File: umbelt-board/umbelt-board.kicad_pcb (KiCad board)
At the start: 4 copper layers, 50.8 x 15.2 mm, 99 parts, among them J1 USB4105-GF-A, J2 Conn_01x06, J3 SM04B-SRSS-TB, J4 TC2050-IDC-NL, J5 BM02B-ACHLKS, J6 Conn_Flex_Motor, J7 Conn_Indiv_Motor, Q1 AO3415A, SW1 KMR231NG-ULC-LFS, SW2 CUS-12TB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

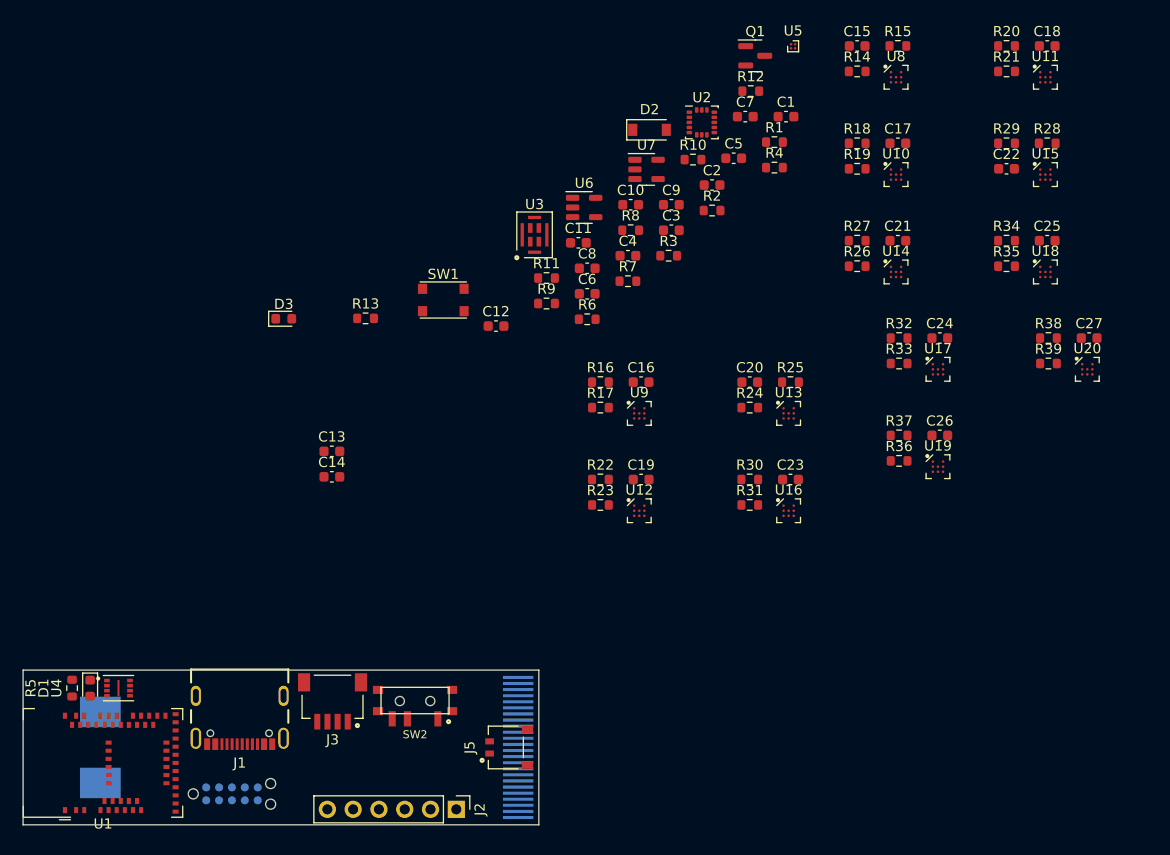
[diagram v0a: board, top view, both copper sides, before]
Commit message: more placement, update custom footprints' ref des on fab layer
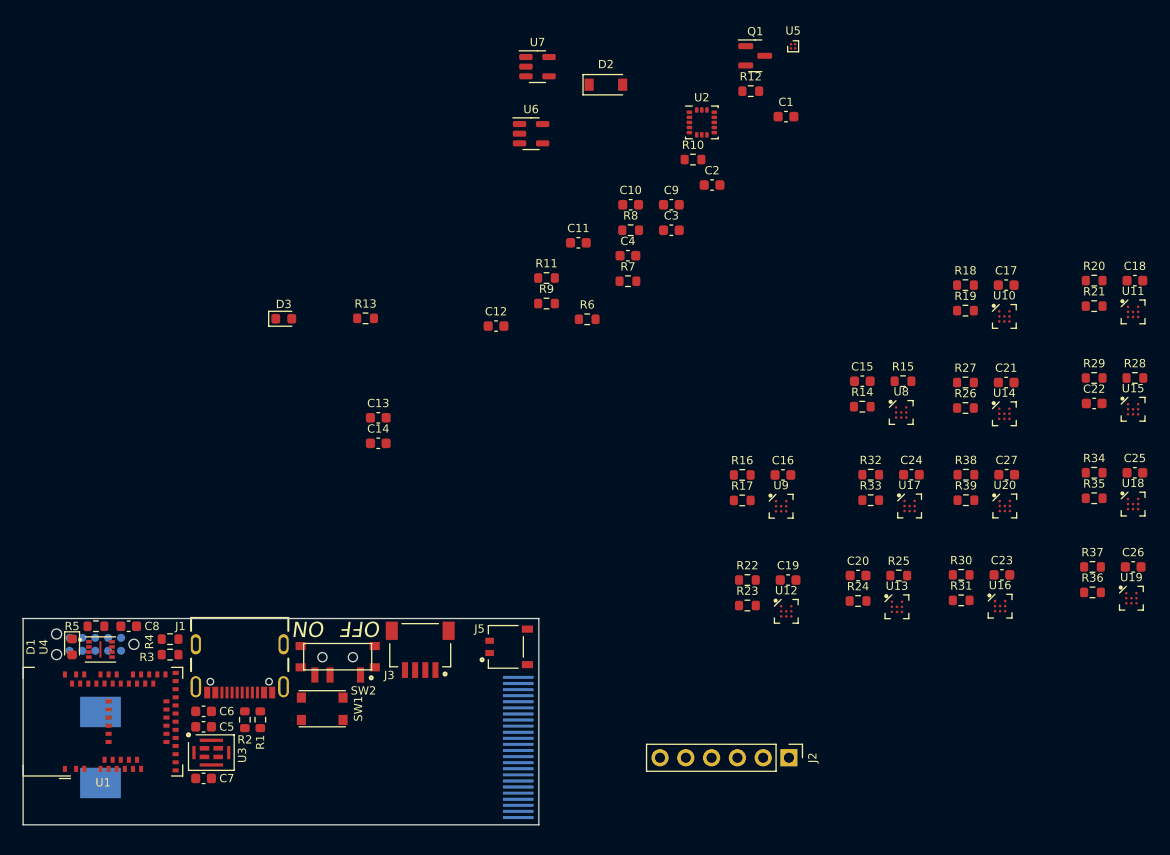
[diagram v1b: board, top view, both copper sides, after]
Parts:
- moved C7 84.2 mm to (144.8, 122.4)
- moved C5 76.6 mm to (144.8, 117.3)
- moved R1 76.2 mm to (150.4, 116.6), turned to 270 degrees
- moved R4 75.5 mm to (141.5, 108.7), turned to 180 degrees
- moved R2 68.1 mm to (148.8, 116.6), turned to 270 degrees
- moved R3 62.9 mm to (141.5, 110.2), turned to 180 degrees
- moved U3 60.1 mm to (145.5, 119.9), turned to 270 degrees
- moved C8 57.3 mm to (137.4, 107.4)
- moved C6 55.9 mm to (144.8, 115.8)
- moved SW1 42.0 mm to (156.5, 115.6)
- moved J2 33.2 mm to (202.4, 120.4)
- moved C15 33.0 mm to (209.7, 83.3)
- moved R15 33.0 mm to (213.7, 83.3)
- moved U8 33.0 mm to (213.5, 86.4)
- moved R14 33.0 mm to (209.7, 85.8)
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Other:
- board size 50.8 x 15.2 mm -> 50.8 x 20.3 mm
- board text added: "OFF"
- board text added: "ON"

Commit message: add SMD pin header, finished placement
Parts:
- J2: footprint Connector_PinHeader_2.54mm:PinHeader_1x06_P2.54mm_Vertical -> umbelt-board:PinHeader_1x06_P2.54mm_Right_Angle_SMD; moved to B.Cu
- moved U5 98.2 mm to (139.7, 125.5)
- moved C27 96.6 mm to (133.1, 125.5), turned to 90 degrees
- moved R38 94.2 mm to (131.6, 125.5), turned to 270 degrees
- moved C18 92.1 mm to (158.5, 122.4), turned to 90 degrees
- moved U20 91.8 mm to (136.9, 125.5), turned to 180 degrees
- moved R39 90.5 mm to (134.6, 125.5), turned to 270 degrees
- moved R20 90.0 mm to (157.0, 122.4), turned to 270 degrees
- moved U11 87.1 mm to (162.3, 122.4), turned to 180 degrees
- moved R21 86.1 mm to (160.0, 122.4), turned to 270 degrees
- moved C1 83.3 mm to (150.2, 122.4), turned to 270 degrees
- moved C17 83.3 mm to (158.5, 125.5), turned to 90 degrees
- moved R18 81.3 mm to (157.0, 125.5), turned to 270 degrees
- moved R15 80.8 mm to (144.8, 125.5), turned to 270 degrees
- moved C15 78.7 mm to (143.3, 125.5), turned to 90 degrees
- moved R14 78.7 mm to (141.7, 125.5), turned to 270 degrees
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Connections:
- net Net-(C12-Pad2) renamed /REGIN
- C10 pad 1: VBUS -> VBAT
- J5 pad 2: VBUS -> VBAT
- Q1 pad 2: VBUS -> VBAT
- R6 pad 1: VBUS -> VBAT
- U7 pad 3: VBUS -> VBAT
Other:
- board size 50.8 x 20.3 mm -> 56.6 x 20.3 mm
- board text added: "CHARGE"
- board text added: "RESET"
- board text added: "UMBELT"

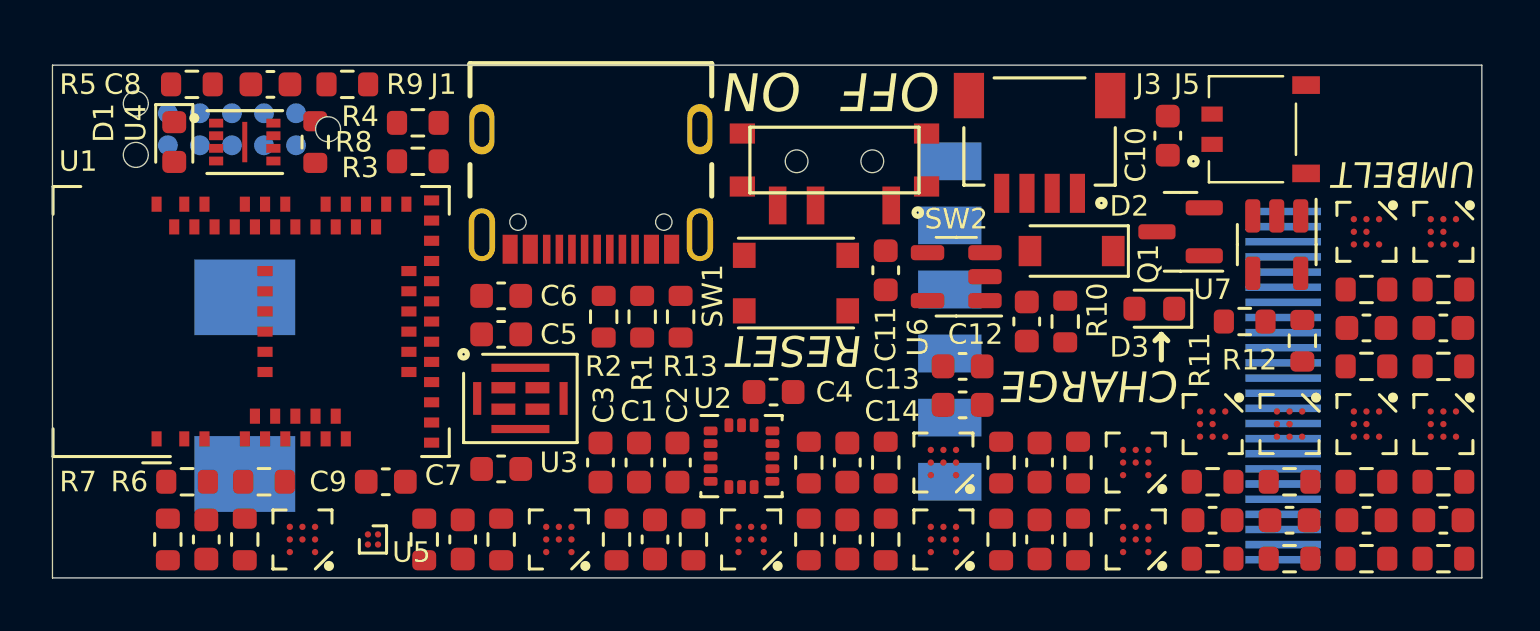
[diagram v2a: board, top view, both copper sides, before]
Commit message: tweak placement, add text, add test points, add rounded corners
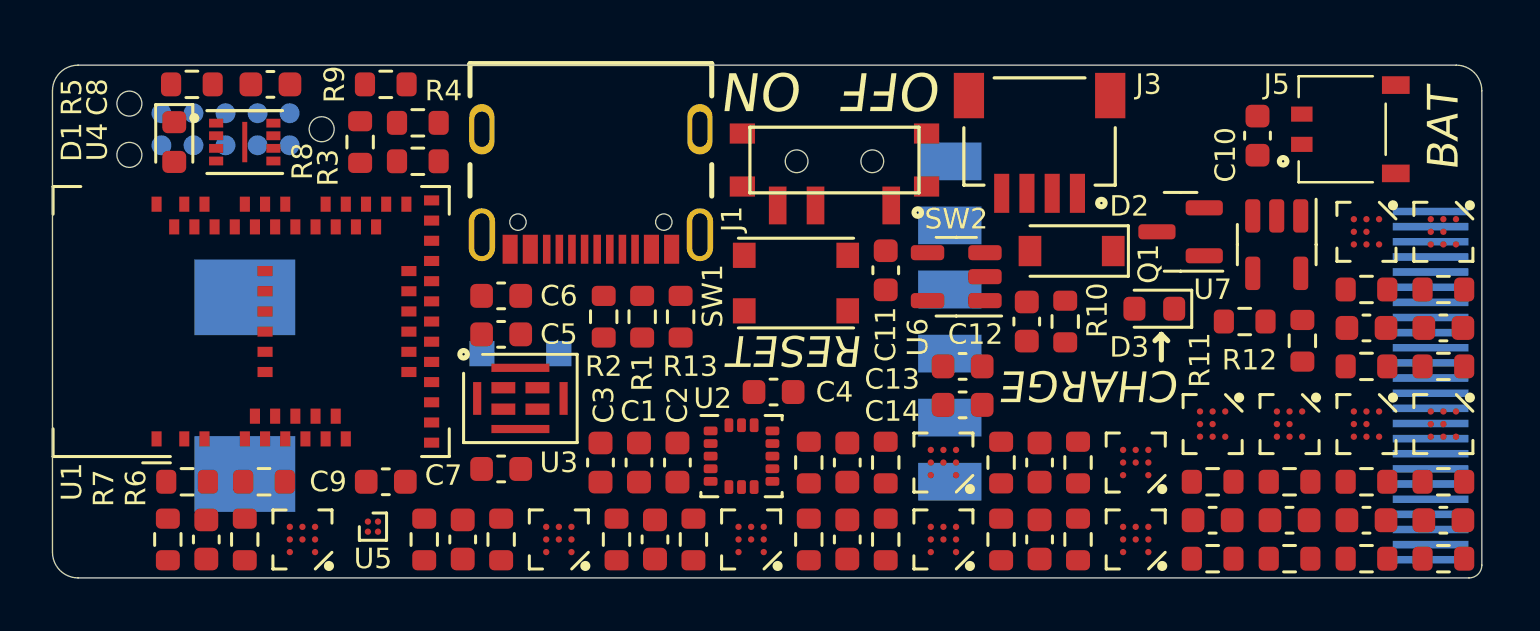
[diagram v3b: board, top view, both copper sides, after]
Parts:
- added TP1: PDM_DAT, TestPoint:TestPoint_Pad_1.0x1.0mm, B.Cu at (144.0, 118.1)
- added TP2: PDM_CLK, TestPoint:TestPoint_Pad_1.0x1.0mm, B.Cu at (147.1, 118.1)
- moved C23 7.62 mm to (179.1, 124.7)
- moved C24 7.62 mm to (182.1, 124.7)
- moved C25 7.62 mm to (179.1, 117.1)
- moved C26 7.62 mm to (182.1, 117.1)
- moved R30 7.62 mm to (179.1, 126.2)
- moved R31 7.62 mm to (179.1, 123.2)
- moved R32 7.62 mm to (182.1, 126.2)
- moved R33 7.62 mm to (182.1, 123.2)
- moved R34 7.62 mm to (179.1, 118.6)
- moved R35 7.62 mm to (179.1, 115.6)
- moved R36 7.62 mm to (182.1, 118.6)
- moved R37 7.62 mm to (182.1, 115.6)
- moved U16 7.62 mm to (179.1, 120.9)
- moved U17 7.62 mm to (182.1, 120.9)
- moved U18 7.62 mm to (179.1, 113.3)
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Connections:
- U1 pad 11: /VDIV -> /A1
- U1 pad 13: /MOTOR_EN_2 -> /MOTOR_EN_5
- U1 pad 14: /MOTOR_EN_1 -> /MOTOR_EN_4
- U1 pad 16: /MOTOR_PWM_1 -> /MOTOR_PWM_0
- U1 pad 17: /MOTOR_PWM_2 -> /MOTOR_PWM_1
- U1 pad 18: /MOTOR_PWM_3 -> /MOTOR_PWM_2
- U1 pad 19: /MOTOR_PWM_4 -> /MOTOR_PWM_3
- U1 pad 20: /MOTOR_PWM_5 -> /MOTOR_PWM_4
- U1 pad 21: /MOTOR_PWM_6 -> /MOTOR_PWM_5
- U1 pad 24: /MOTOR_PWM_7 -> /MOTOR_PWM_6
- U1 pad 25: /MOTOR_PWM_8 -> /MOTOR_PWM_7
- U1 pad 26: /MOTOR_PWM_9 -> /MOTOR_PWM_8
- U1 pad 36: /MOTOR_PWM_10 -> /MOTOR_PWM_9
- U1 pad 37: /MOTOR_PWM_11 -> /MOTOR_PWM_10
- U1 pad 38: /MOTOR_PWM_12 -> /MOTOR_PWM_11
- U1 pad 39: /MOTOR_PWM_0 -> /MOTOR_PWM_12
- U1 pad 4: /MOTOR_EN_8 -> /MOTOR_EN_0
- U1 pad 5: /MOTOR_EN_7 -> Net-(U1-Pad5)
- U1 pad 56: Net-(U1-Pad56) -> /MOTOR_EN_7
- U1 pad 57: /MOTOR_EN_0 -> /MOTOR_EN_8
- U1 pad 58: /MOTOR_EN_12 -> /MOTOR_EN_9
- U1 pad 59: /MOTOR_EN_11 -> /MOTOR_EN_10
- U1 pad 6: /MOTOR_EN_6 -> /MOTOR_EN_1
- U1 pad 60: /MOTOR_EN_10 -> /MOTOR_EN_11
- U1 pad 61: /MOTOR_EN_9 -> /MOTOR_EN_12
- U1 pad 7: /MOTOR_EN_5 -> /MOTOR_EN_6
- U1 pad 8: /MOTOR_EN_4 -> /MOTOR_EN_2
- U1 pad 9: /A1 -> /VDIV
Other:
- outline, holes or cut-outs redrawn
- board text added: "3.3V"
- board text added: "3.5-6V INPUT"
- board text added: "A0"
- board text added: "A1"
- board text added: "BAT"
- board text added: "D0"
- board text added: "D1"
- board text added: "GND"
- board text added: "M. Pauly"
- board text added: "MOTOR 0"
- board text added: "N. Cygan"
- board text added: "PDM_CLK"
- board text added: "PDM_DAT"
- board text added: "PROG"
- board text added: "V1.0"

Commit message: lots of routing; hard part done
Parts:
- moved J6 3.81 mm to (177.8, 119.4)
- moved J2 2.03 mm to (162.6, 114.8)
- moved R3 1.52 mm to (141.5, 109.0)
- moved R4 1.52 mm to (141.5, 110.5)
- moved C13 0.13 mm to (163.1, 118.5)
- moved C14 0.13 mm to (163.1, 120.0)
- turned R14 to 90 degrees
- turned R16 to 90 degrees
- turned R18 to 90 degrees
- turned R20 to 90 degrees
- turned R22 to 90 degrees
- turned R24 to 90 degrees
- turned R28 to 180 degrees
- turned R30 to 180 degrees
- turned R32 to 180 degrees
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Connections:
- net Net-(J1-PadA6) renamed /D+
- net Net-(J1-PadA7) renamed /D-
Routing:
- net GND: track 0.00 -> 66.9 mm, vias 0 -> 23
- net VBUS: track 0.00 -> 54.1 mm
- net VBAT: track 0.00 -> 52.5 mm, vias 0 -> 2
- net /motor_drivers/OUT+_1: track 0.00 -> 38.2 mm, vias 0 -> 1
- net /motor_drivers/OUT+_3: track 0.00 -> 38.1 mm, vias 0 -> 2
- net +3V3: track 0.00 -> 36.8 mm, vias 0 -> 15
- net /motor_drivers/OUT-_1: track 0.00 -> 31.4 mm, vias 0 -> 1
- net /motor_drivers/OUT+_2: track 0.00 -> 30.8 mm, vias 0 -> 1
- net /motor_drivers/OUT+_4: track 0.00 -> 30.0 mm, vias 0 -> 1
- net /motor_drivers/OUT-_2: track 0.00 -> 28.8 mm, vias 0 -> 1
- net /motor_drivers/OUT-_3: track 0.00 -> 26.8 mm, vias 0 -> 2
- net /motor_drivers/OUT+_8: track 0.00 -> 23.8 mm, vias 0 -> 1
- net /motor_drivers/OUT+_6: track 0.00 -> 22.5 mm, vias 0 -> 1
- net /motor_drivers/OUT-_8: track 0.00 -> 20.3 mm, vias 0 -> 1
- net /motor_drivers/OUT+_5: track 0.00 -> 19.8 mm, vias 0 -> 2
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- added copper zone on B.Cu, net GND
- added copper zone on F.Cu, net GND
- added copper zone on In1.Cu, net GND
- added copper zone on In2.Cu, net GND
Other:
- net class USB added: clearance 0.1524, trace_width 0.1524, via_dia 0.6096, via_drill 0.3048

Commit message: more routing
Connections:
- J2 pad 3: /A0 -> /D0
- J2 pad 4: /A1 -> /D1
- J2 pad 5: /D0 -> /A0
- J2 pad 6: /D1 -> /A1
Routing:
- net +3V3: track 36.8 -> 239.8 mm, vias 15 -> 23
- net /MOTOR_EN_10: track 0.98 -> 65.1 mm, vias 1 -> 2
- net /MOTOR_EN_9: track 6.99 -> 69.8 mm, vias 1 -> 2
- net /MOTOR_EN_12: track 1.58 -> 62.8 mm, vias 1 -> 2
- net /MOTOR_PWM_7: track 0.99 -> 58.4 mm, vias 1 -> 3
- net /MOTOR_PWM_10: track 0.00 -> 56.9 mm, vias 0 -> 2
- net /MOTOR_EN_11: track 2.36 -> 58.4 mm, vias 1 -> 2
- net /SDA: track 0.00 -> 55.7 mm, vias 0 -> 5
- net /MOTOR_PWM_9: track 0.19 -> 55.4 mm, vias 1 -> 2
- net /SCL: track 0.00 -> 55.0 mm, vias 0 -> 5
- net /MOTOR_PWM_12: track 0.61 -> 53.0 mm, vias 1 -> 2
- net /MOTOR_PWM_11: track 0.15 -> 51.8 mm, vias 1 -> 2
- net /MOTOR_EN_5: track 1.92 -> 48.0 mm, vias 1 -> 2
- net /MOTOR_EN_6: track 2.73 -> 48.4 mm, vias 1 -> 2
- net /MOTOR_PWM_8: track 16.4 -> 55.9 mm, vias 1 -> 2
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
